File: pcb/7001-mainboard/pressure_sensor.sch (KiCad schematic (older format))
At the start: 24 parts, among them U1 MPRLS0001PG0000SA, U10 ABPMAND001PG2A3, U11 MPVZ5010GW6U, U12 MPVZ5010GW6U, U8 MPRLS0001PG0000SA, U9 ABPMAND001PG2A3

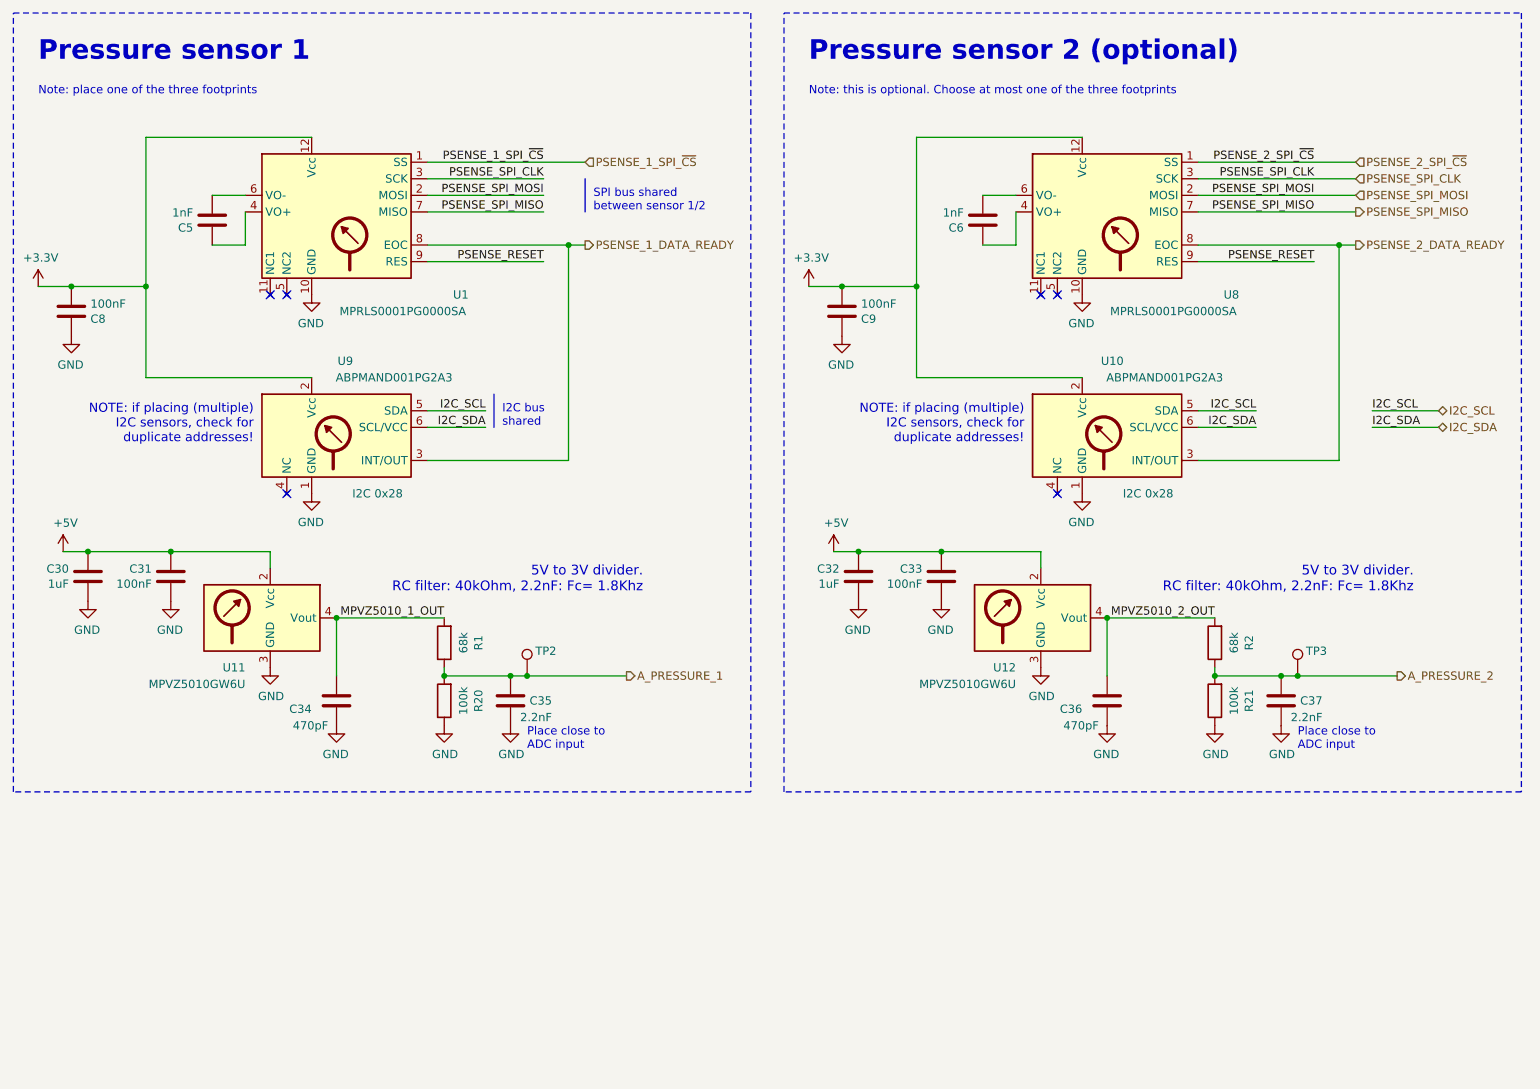
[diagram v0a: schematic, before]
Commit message: Schematics: add 24v,12v power supplies, etc
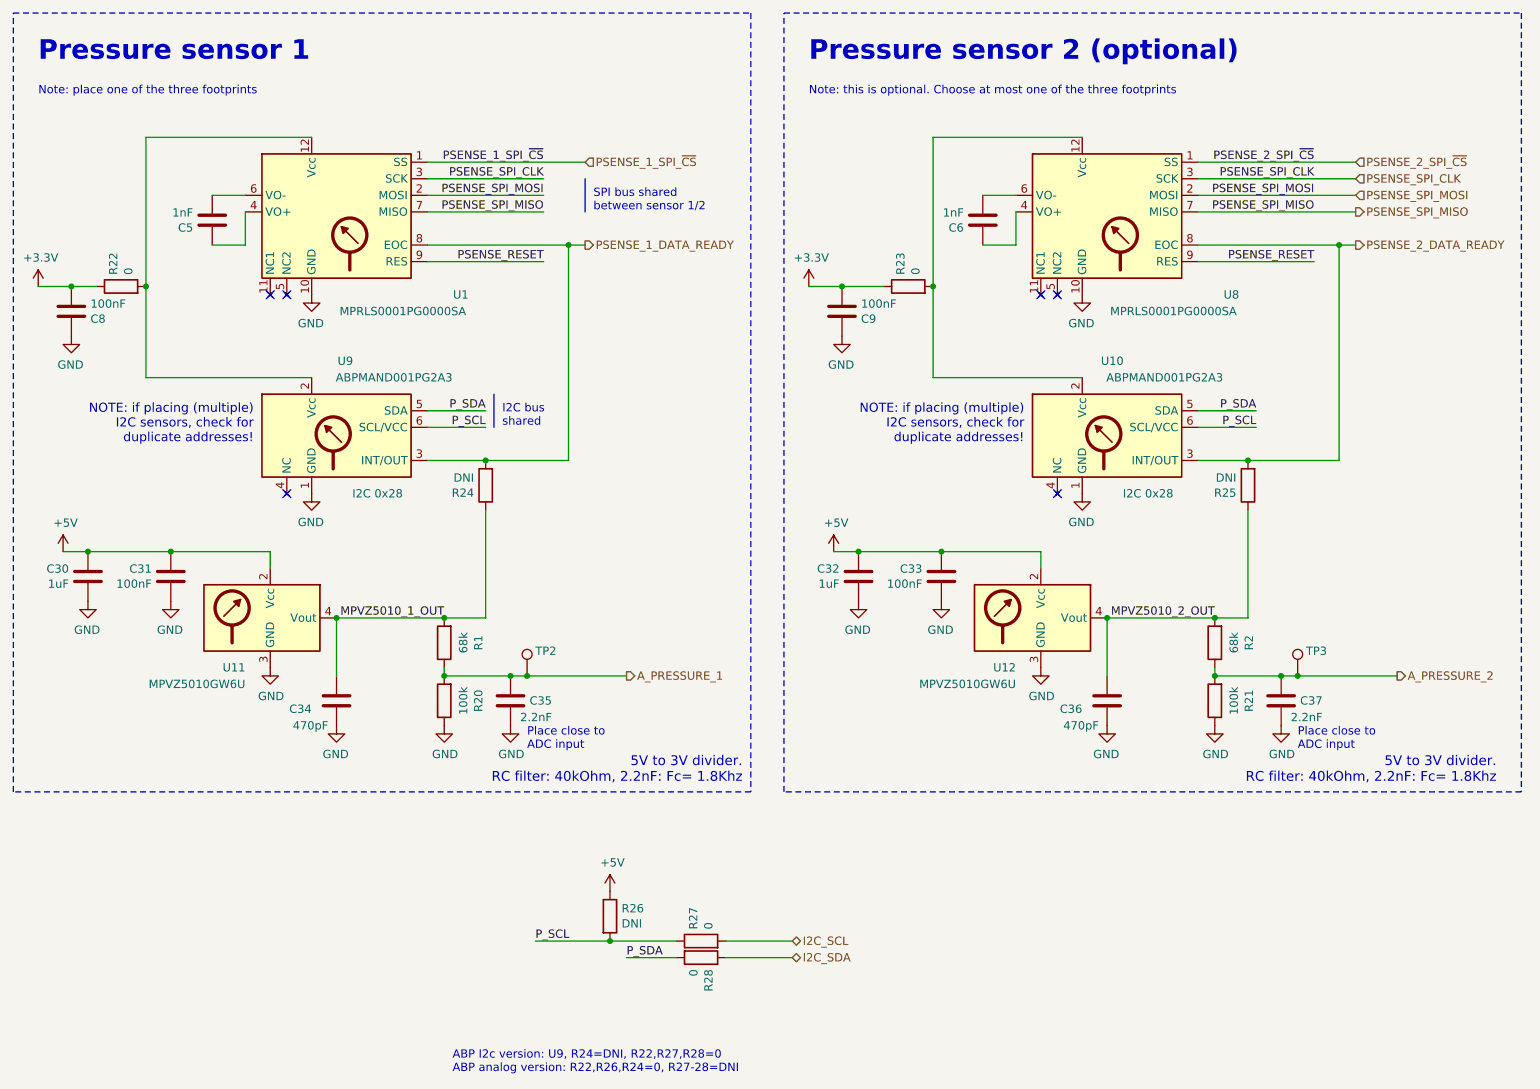
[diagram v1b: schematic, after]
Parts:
- added R22, R23, R27, R28: 0, Resistor_SMD:R_0805_2012Metric, symbol Device:R
- added R24, R25, R26: DNI, Resistor_SMD:R_0805_2012Metric, symbol Device:R
- U10: footprint Jitter_Footprints:ABPMXXX000XX0XX -> Jitter_Footprints:ABPM+DXXX000XX0XX
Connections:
- net +3V3: now also R22.1, R23.1; no longer U1.12 (Vcc), U10.2 (Vcc), U8.12 (Vcc), U9.2 (Vcc)
- net +5V: now also R26.1
- net I2C_SCL: now also R27.2; no longer U10.5 (SDA), U9.5 (SDA)
- net I2C_SDA: now also R28.1; no longer U10.6 (SCL/VCC), U9.6 (SCL/VCC)
- net MPVZ5010_1_OUT: now also R24.1
- net MPVZ5010_2_OUT: now also R25.1
- net PSENSE_1_DATA_READY: now also R24.2
- net PSENSE_2_DATA_READY: now also R25.2
- new net: R23.2, U10.2 (Vcc), U8.12 (Vcc)
- new net: R22.2, U1.12 (Vcc), U9.2 (Vcc)
- new net P_SCL: R26.2, R27.1, U10.6 (SCL/VCC), U9.6 (SCL/VCC)
- new net P_SDA: R28.2, U10.5 (SDA), U9.5 (SDA)
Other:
- note added: "ABP I2c version: U9, R24=DNI, R22,R27,R28=0\nABP analog version: R22,R26,R24=0, R27-28=DNI"
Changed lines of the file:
@@
 Wire Wire Line
 	1400 2750 1600 2750
-Connection ~ 1600 2750
-Wire Wire Line
-	1600 2750 2050 2750
 $Comp
 L Jitter_Components:ABPMXXX000XX0XX U?
@@
 	-1   0    0    -1
 $EndComp
-Text Label 4100 3500 2    50   ~ 0
-I2C_SCL
-Text Label 4100 3600 2    50   ~ 0
-I2C_SDA
 Wire Wire Line
 	4100 3500 3750 3500
@@
 	4250 5100 4350 5100
 Connection ~ 4250 5100
-Text Notes 5050 4600 2    59   ~ 0
+Text Notes 5650 5750 2    59   ~ 0
 5V to 3V divider.\nRC filter: 40kOhm, 2.2nF: Fc= 1.8Khz\n
 $Comp
@@
 	4600 3800 4600 2500
 Wire Wire Line
-	4600 3800 3750 3800
+	4600 3800 4100 3800
 Wire Wire Line
 	4700 2500 4600 2500
@@
 	3050 3300 2050 3300
 Wire Wire Line
-	2050 3300 2050 2750
-Wire Wire Line
 	2050 1850 3050 1850
-Connection ~ 2050 2750
-Wire Wire Line
-	2050 2750 2050 1850
 Text Notes 1400 1600 0    50   ~ 0
 Note: place one of the three footprints
@@
 Wire Wire Line
 	6050 2750 6250 2750
-Connection ~ 6250 2750
-Wire Wire Line
-	6250 2750 6700 2750
 $Comp
 L Jitter_Components:ABPMXXX000XX0XX U?
@@
 F 0 "U10" H 7450 4200 50  0000 L CNN
 F 1 "ABPMAND001PG2A3" H 6850 4100 50  0000 L CNN
-F 2 "Jitter_Footprints:ABPMXXX000XX0XX" H 7800 3600 50  0001 C CNN
+F 2 "Jitter_Footprints:ABPM+DXXX000XX0XX" H 7800 3600 50  0001 C CNN
 F 3 "https://nl.mouser.com/datasheet/2/187/honeywell-sensing-basic-board-mount-pressure-abp-s-916690.pdf" H 7800 3700 50  0001 C CNN
 F 4 "I2C 0x28" H 7150 3400 50  0000 L CNN "Interface"
@@
 	-1   0    0    -1
 $EndComp
-Text Label 8750 3500 2    50   ~ 0
-I2C_SCL
-Text Label 8750 3600 2    50   ~ 0
-I2C_SDA
 Wire Wire Line
 	8750 3500 8400 3500
@@
 	8900 5100 9000 5100
 Connection ~ 8900 5100
-Text Notes 9700 4600 2    59   ~ 0
+Text Notes 10200 5750 2    59   ~ 0
 5V to 3V divider.\nRC filter: 40kOhm, 2.2nF: Fc= 1.8Khz\n
 $Comp
@@
 	9250 3800 9250 2500
 Wire Wire Line
-	9250 3800 8400 3800
+	9250 3800 8700 3800
 Wire Wire Line
 	9350 2500 9250 2500
 Connection ~ 9250 2500
 Wire Wire Line
-	7700 3300 6700 3300
-Wire Wire Line
-	6700 3300 6700 2750
-Wire Wire Line
-	6700 1850 7700 1850
-Connection ~ 6700 2750
-Wire Wire Line
-	6700 2750 6700 1850
+	7700 3300 6800 3300
+Wire Wire Line
+	6800 1850 7700 1850
 Text Notes 6050 1600 0    50   ~ 0
 Note: this is optional. Choose at most one of the three footprints
@@
 Text HLabel 4700 2500 2    50   Output ~ 0
 PSENSE_1_DATA_READY
-Text Label 9450 3500 0    50   ~ 0
+Text Label 4400 6700 0    50   ~ 0
+P_SCL
+Text Label 4950 6800 0    50   ~ 0
+P_SDA
+Text HLabel 5950 6700 2    50   BiDi ~ 0
 I2C_SCL
-Text Label 9450 3600 0    50   ~ 0
+Wire Wire Line
+	5950 6700 5550 6700
+Text HLabel 5950 6800 2    50   BiDi ~ 0
 I2C_SDA
-Text HLabel 9850 3500 2    50   BiDi ~ 0
-I2C_SCL
-Wire Wire Line
-	9850 3500 9450 3500
-Text HLabel 9850 3600 2    50   BiDi ~ 0
-I2C_SDA
-Wire Wire Line
-	9450 3600 9850 3600
+Wire Wire Line
+	5550 6800 5950 6800
 Text Notes 4200 3600 0    50   ~ 0
 I2C bus\nshared
@@
 	4950 5100 4350 5100
 Connection ~ 4350 5100
+$Comp
+L Device:R R?
+U 1 1 5E7A0096
+P 6650 2750
+AR Path="/5BF2E340/5E7A0096" Ref="R?"  Part="1"
+AR Path="/5E7A0096" Ref="R?"  Part="1"
+AR Path="/5F5B6035/5E7A0096" Ref="R23"  Part="1"
+F 0 "R23" H 6720 2796 50  0000 L CNN
+F 1 "0" H 6720 2705 50  0000 L CNN
+F 2 "Resistor_SMD:R_0805_2012Metric" V 6580 2750 50  0001 C CNN
+F 3 "~" H 6650 2750 50  0001 C CNN
+	1    6650 2750
+	0    -1   -1   0
+$EndComp
+Wire Wire Line
+	6800 1850 6800 2750
+Connection ~ 6800 2750
+Wire Wire Line
+	6800 2750 6800 3300
+Wire Wire Line
+	6500 2750 6250 2750
+Connection ~ 6250 2750
+$Comp
+L Device:R R?
+U 1 1 5E7A5311
+P 1900 2750
+AR Path="/5BF2E340/5E7A5311" Ref="R?"  Part="1"
+AR Path="/5E7A5311" Ref="R?"  Part="1"
+AR Path="/5F5B6035/5E7A5311" Ref="R22"  Part="1"
+F 0 "R22" H 1970 2796 50  0000 L CNN
+F 1 "0" H 1970 2705 50  0000 L CNN
+F 2 "Resistor_SMD:R_0805_2012Metric" V 1830 2750 50  0001 C CNN
+F 3 "~" H 1900 2750 50  0001 C CNN
+	1    1900 2750
+	0    -1   -1   0
+$EndComp
+Wire Wire Line
+	2050 1850 2050 2750
+Connection ~ 2050 2750
+Wire Wire Line
+	2050 2750 2050 3300
+Wire Wire Line
+	1750 2750 1600 2750
+Connection ~ 1600 2750
+$Comp
+L Device:R R?
+U 1 1 5E7A758F
+P 8700 3950
+AR Path="/5BF2E340/5E7A758F" Ref="R?"  Part="1"
+AR Path="/5E7A758F" Ref="R?"  Part="1"
+AR Path="/5F5B6035/5E7A758F" Ref="R25"  Part="1"
+F 0 "R25" H 8770 3996 50  0000 L CNN
+F 1 "DNI" H 8770 3905 50  0000 L CNN
+F 2 "Resistor_SMD:R_0805_2012Metric" V 8630 3950 50  0001 C CNN
+F 3 "~" H 8700 3950 50  0001 C CNN
+	1    8700 3950
+	-1   0    0    1
+$EndComp
+Connection ~ 8700 3800
+Wire Wire Line
+	8700 3800 8400 3800
+Wire Wire Line
+	8700 4100 8700 4750
+Wire Wire Line
+	8700 4750 8500 4750
+Connection ~ 8500 4750
+$Comp
+L Device:R R?
+U 1 1 5E7AB07D
+P 4100 3950
+AR Path="/5BF2E340/5E7AB07D" Ref="R?"  Part="1"
+AR Path="/5E7AB07D" Ref="R?"  Part="1"
+AR Path="/5F5B6035/5E7AB07D" Ref="R24"  Part="1"
+F 0 "R24" H 4170 3996 50  0000 L CNN
+F 1 "DNI" H 4170 3905 50  0000 L CNN
+F 2 "Resistor_SMD:R_0805_2012Metric" V 4030 3950 50  0001 C CNN
+F 3 "~" H 4100 3950 50  0001 C CNN
+	1    4100 3950
+	-1   0    0    1
+$EndComp
+Wire Wire Line
+	4100 4100 4100 4750
+Wire Wire Line
+	4100 4750 3850 4750
+Connection ~ 3850 4750
+Connection ~ 4100 3800
+Wire Wire Line
+	4100 3800 3750 3800
+$Comp
+L Device:R R?
+U 1 1 5E7B1850
+P 5400 6700
+AR Path="/5BF2E340/5E7B1850" Ref="R?"  Part="1"
+AR Path="/5E7B1850" Ref="R?"  Part="1"
+AR Path="/5F5B6035/5E7B1850" Ref="R27"  Part="1"
+F 0 "R27" H 5470 6746 50  0000 L CNN
+F 1 "0" H 5470 6655 50  0000 L CNN
+F 2 "Resistor_SMD:R_0805_2012Metric" V 5330 6700 50  0001 C CNN
+F 3 "~" H 5400 6700 50  0001 C CNN
+	1    5400 6700
+	0    -1   -1   0
+$EndComp
+$Comp
+L Device:R R?
+U 1 1 5E7B1DA5
+P 5400 6800
+AR Path="/5BF2E340/5E7B1DA5" Ref="R?"  Part="1"
+AR Path="/5E7B1DA5" Ref="R?"  Part="1"
+AR Path="/5F5B6035/5E7B1DA5" Ref="R28"  Part="1"
+F 0 "R28" H 5470 6846 50  0000 L CNN
+F 1 "0" H 5470 6755 50  0000 L CNN
+F 2 "Resistor_SMD:R_0805_2012Metric" V 5330 6800 50  0001 C CNN
+F 3 "~" H 5400 6800 50  0001 C CNN
+	1    5400 6800
+	0    1    1    0
+$EndComp
+Wire Wire Line
+	4950 6800 5250 6800
+Wire Wire Line
+	4400 6700 4850 6700
+Text Label 4100 3600 2    50   ~ 0
+P_SCL
+Text Label 4100 3500 2    50   ~ 0
+P_SDA
+Text Label 8750 3500 2    50   ~ 0
+P_SDA
+Text Label 8750 3600 2    50   ~ 0
+P_SCL
+$Comp
+L Device:R R?
+U 1 1 5E7B6BB2
+P 4850 6550
+AR Path="/5BF2E340/5E7B6BB2" Ref="R?"  Part="1"
+AR Path="/5E7B6BB2" Ref="R?"  Part="1"
+AR Path="/5F5B6035/5E7B6BB2" Ref="R26"  Part="1"
+F 0 "R26" H 4920 6596 50  0000 L CNN
+F 1 "DNI" H 4920 6505 50  0000 L CNN
+F 2 "Resistor_SMD:R_0805_2012Metric" V 4780 6550 50  0001 C CNN
+F 3 "~" H 4850 6550 50  0001 C CNN
+	1    4850 6550
+	1    0    0    -1
+$EndComp
+Connection ~ 4850 6700
+Wire Wire Line
+	4850 6700 5250 6700
+$Comp
+L power:+5V #PWR?
+U 1 1 5E7B8980
+P 4850 6400
+AR Path="/5BF41E5D/5E7B8980" Ref="#PWR?"  Part="1"
+AR Path="/5E7B8980" Ref="#PWR?"  Part="1"
+AR Path="/5F5B6035/5E7B8980" Ref="#PWR023"  Part="1"
+F 0 "#PWR023" H 4850 6250 50  0001 C CNN
+F 1 "+5V" H 4865 6573 50  0000 C CNN
+F 2 "" H 4850 6400 50  0001 C CNN
+F 3 "" H 4850 6400 50  0001 C CNN
+	1    4850 6400
+	1    0    0    -1
+$EndComp
+Text Notes 3900 7500 0    50   ~ 0
+ABP I2c version: U9, R24=DNI, R22,R27,R28=0\nABP analog version: R22,R26,R24=0, R27-28=DNI
 $EndSCHEMATC

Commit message: Cleanup BOM, sync with schematic, prepare layout
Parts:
- TP2, TP3: value TestPoint -> DNI
- U1, U8: Digikey (none) -> 480-7100-1-ND; MPN (none) -> MPRLS0001PG0000SA
- U9: footprint Jitter_Footprints:ABPMXXX000XX0XX -> Jitter_Footprints:ABPM+DXXX000XX0XX
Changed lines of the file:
@@
 F 2 "Jitter_Footprints:MPRLS0001PG0000SA" H 3150 2500 50  0001 C CNN
 F 3 "http://www.honeywellscportal.com//index.php?ci_id=138832" H 3150 2500 50  0001 C CNN
+F 4 "480-7100-1-ND" H 3050 2500 50  0001 C CNN "Digikey"
+F 5 "MPRLS0001PG0000SA" H 3050 2500 50  0001 C CNN "MPN"
 	1    3050 2500
 	-1   0    0    -1
@@
 F 0 "U9" H 2800 4200 50  0000 L CNN
 F 1 "ABPMAND001PG2A3" H 2200 4100 50  0000 L CNN
-F 2 "Jitter_Footprints:ABPMXXX000XX0XX" H 3150 3600 50  0001 C CNN
+F 2 "Jitter_Footprints:ABPM+DXXX000XX0XX" H 3150 3600 50  0001 C CNN
 F 3 "https://nl.mouser.com/datasheet/2/187/honeywell-sensing-basic-board-mount-pressure-abp-s-916690.pdf" H 3150 3700 50  0001 C CNN
 F 4 "I2C 0x28" H 2500 3400 50  0000 L CNN "Interface"
@@
 AR Path="/5F5B6035/5F5C762B" Ref="TP2"  Part="1"
 F 0 "TP2" H 4400 5250 50  0000 L CNN
-F 1 "TestPoint" H 4400 5250 50  0001 L CNN
+F 1 "DNI" H 4400 5250 50  0001 L CNN
 F 2 "TestPoint:TestPoint_THTPad_D1.5mm_Drill0.7mm" H 4550 5100 50  0001 C CNN
 F 3 "~" H 4550 5100 50  0001 C CNN
@@
 F 2 "Jitter_Footprints:MPRLS0001PG0000SA" H 7800 2500 50  0001 C CNN
 F 3 "http://www.honeywellscportal.com//index.php?ci_id=138832" H 7800 2500 50  0001 C CNN
+F 4 "MPRLS0001PG0000SA" H 7700 2500 50  0001 C CNN "MPN"
+F 5 "480-7100-1-ND" H 7700 2500 50  0001 C CNN "Digikey"
 	1    7700 2500
 	-1   0    0    -1
@@
 AR Path="/5F5B6035/5F5FFBB8" Ref="TP3"  Part="1"
 F 0 "TP3" H 9050 5250 50  0000 L CNN
-F 1 "TestPoint" H 9050 5250 50  0001 L CNN
+F 1 "DNI" H 9050 5250 50  0001 L CNN
 F 2 "TestPoint:TestPoint_THTPad_D1.5mm_Drill0.7mm" H 9200 5100 50  0001 C CNN
 F 3 "~" H 9200 5100 50  0001 C CNN

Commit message: Update schematics based on more feedback
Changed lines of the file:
@@
 	1    0    0    -1
 $EndComp
-Text Notes 3900 7500 0    50   ~ 0
+Text Notes 4350 7200 0    50   ~ 0
 ABP I2c version: U9, R24=DNI, R22,R27,R28=0\nABP analog version: R22,R26,R24=0, R27-28=DNI
+Text Label 8550 1800 0    50   ~ 0
+PSENSE_RESET
+Text HLabel 9350 1800 2    50   Input ~ 0
+PSENSE_RESET
+Wire Wire Line
+	8550 1800 9350 1800
 $EndSCHEMATC

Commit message: PCB: Halfway layouting
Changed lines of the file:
@@
 $EndComp
 Wire Wire Line
-	6800 1850 6800 2750
+	6800 1850 6800 2150
 Connection ~ 6800 2750
 Wire Wire Line
@@
 $EndComp
 Wire Wire Line
-	2050 1850 2050 2750
+	2050 1850 2050 2100
 Connection ~ 2050 2750
 Wire Wire Line
@@
 Wire Wire Line
 	8550 1800 9350 1800
+$Comp
+L power:PWR_FLAG #FLG0103
+U 1 1 6074E056
+P 6800 2150
+F 0 "#FLG0103" H 6800 2225 50  0001 C CNN
+F 1 "PWR_FLAG" V 6800 2277 50  0000 L CNN
+F 2 "" H 6800 2150 50  0001 C CNN
+F 3 "~" H 6800 2150 50  0001 C CNN
+	1    6800 2150
+	0    -1   -1   0
+$EndComp
+Connection ~ 6800 1850
+Connection ~ 6800 2150
+Wire Wire Line
+	6800 2150 6800 2750
+$Comp
+L power:PWR_FLAG #FLG0104
+U 1 1 6074F209
+P 2050 2100
+F 0 "#FLG0104" H 2050 2175 50  0001 C CNN
+F 1 "PWR_FLAG" V 2050 2227 50  0000 L CNN
+F 2 "" H 2050 2100 50  0001 C CNN
+F 3 "~" H 2050 2100 50  0001 C CNN
+	1    2050 2100
+	0    -1   -1   0
+$EndComp
+Connection ~ 2050 2100
+Wire Wire Line
+	2050 2100 2050 2750
 $EndSCHEMATC
